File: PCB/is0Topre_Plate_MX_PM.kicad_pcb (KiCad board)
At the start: 2 copper layers, 29.3 x 51.1 mm, 2 parts

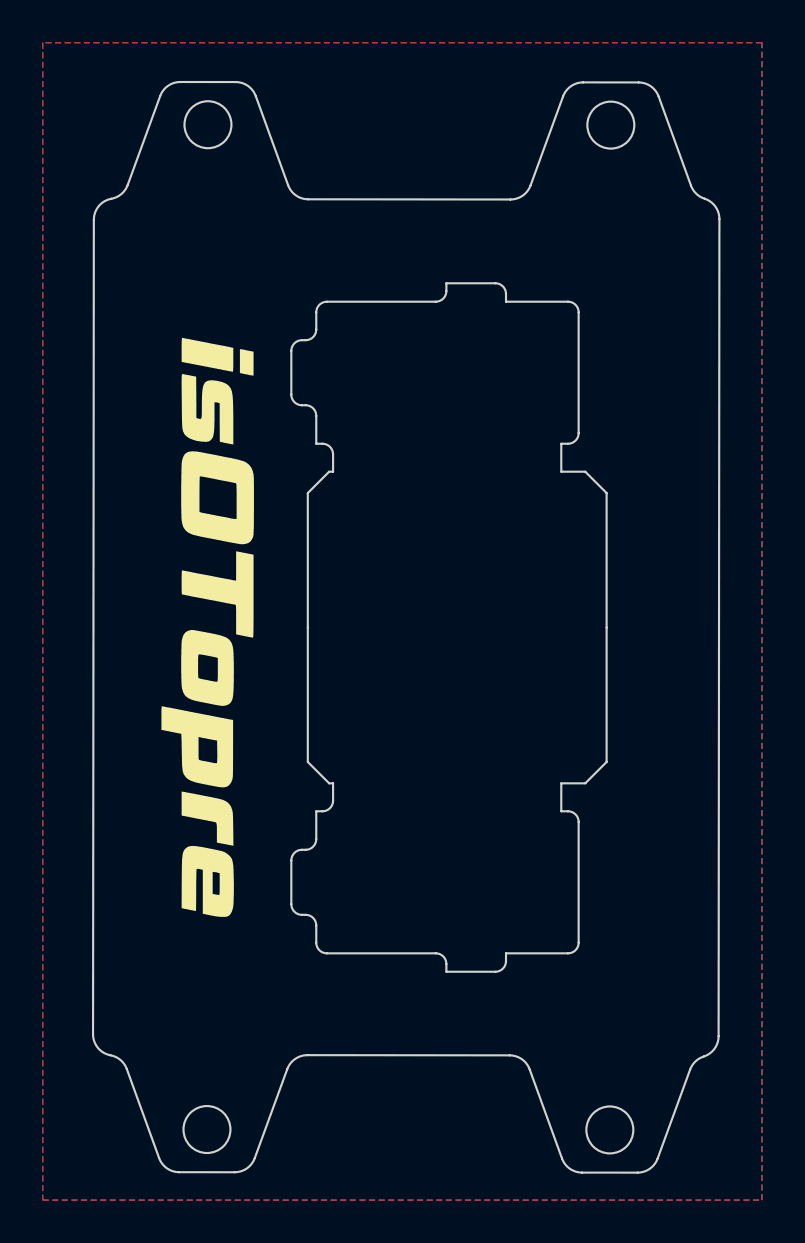
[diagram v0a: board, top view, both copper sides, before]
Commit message: Update to add tape silkscreen
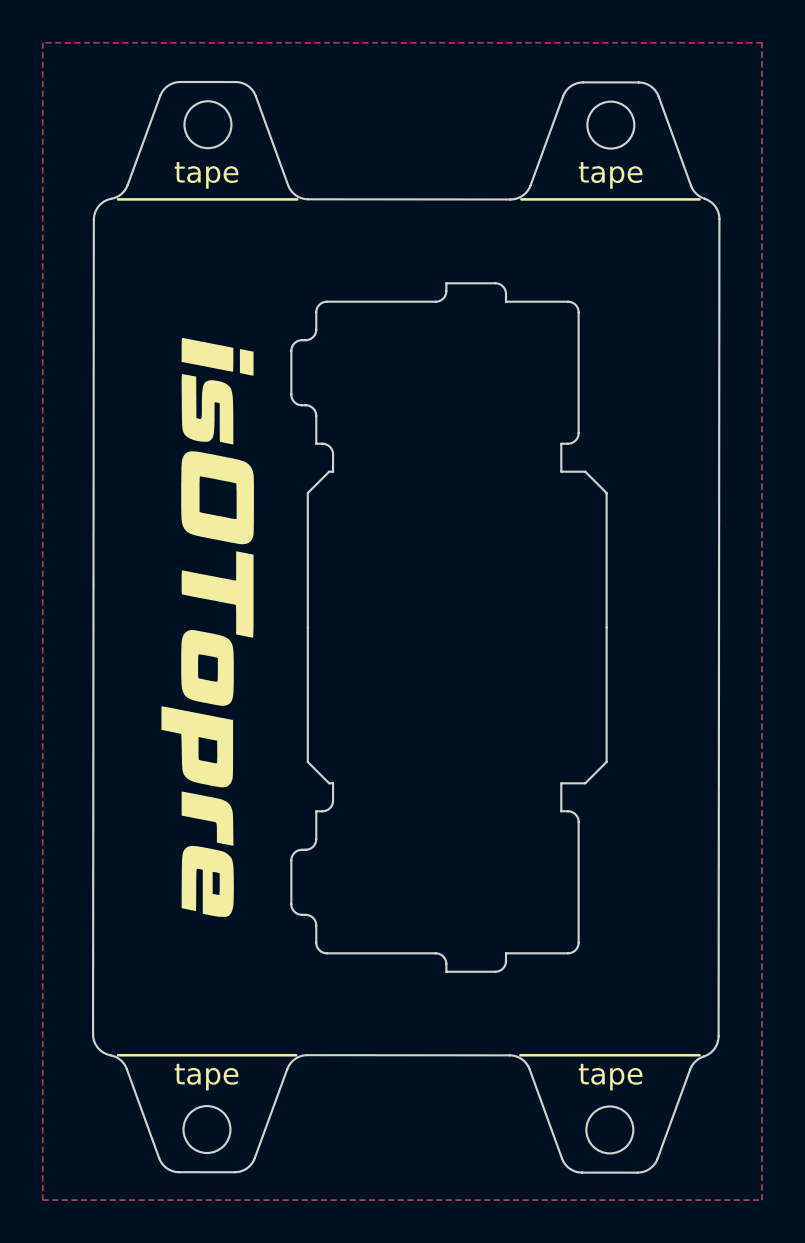
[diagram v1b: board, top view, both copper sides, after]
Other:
- board text added: "tape"
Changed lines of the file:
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@@
       ) (layer "B.SilkS") (width 0.01) (fill solid))
   )
+  (gr_line (start 99.82875 87.35125) (end 91.47875 87.35125) (layer "F.SilkS") (width 0.12))
+  (gr_line (start 110.32875 87.35125) (end 118.72875 87.35125) (layer "F.SilkS") (width 0.12))
+  (gr_line (start 99.87875 47.25125) (end 91.47875 47.25125) (layer "F.SilkS") (width 0.12))
+  (gr_line (start 110.37875 47.25125) (end 118.72875 47.25125) (layer "F.SilkS") (width 0.12))
   (gr_line (start 109.658291 52.044269) (end 112.561891 52.044269) (layer "Edge.Cuts") (width 0.1))
   (gr_arc (start 112.33199 42.42563) (mid 112.69857 41.948854) (end 113.272331 41.768576) (layer "Edge.Cuts") (width 0.1))
@@
     (effects (font (size 1 1) (thickness 0.15)) (justify mirror))
   )
+  (gr_text "tape\n" (at 95.647231 88.25125) (layer "F.SilkS")
+    (effects (font (size 1 1) (thickness 0.15)))
+  )
+  (gr_text "tape\n" (at 114.57875 88.25125) (layer "F.SilkS")
+    (effects (font (size 1 1) (thickness 0.15)))
+  )
+  (gr_text "tape\n" (at 95.647231 46.00125) (layer "F.SilkS")
+    (effects (font (size 1 1) (thickness 0.15)))
+  )
+  (gr_text "tape\n" (at 114.57875 46.00125) (layer "F.SilkS")
+    (effects (font (size 1 1) (thickness 0.15)))
+  )
   (zone (net 0) (net_name "") (layers F&B.Cu) (hatch edge 0.508)
